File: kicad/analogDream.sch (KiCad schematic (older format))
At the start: 120 parts, among them P1 CONN_4X2, P10 CONN_7X2, P11 CONN_4X2, P12 CONN_4X2, P2 CONN_4X2, P3 CONN_7X2, P4 CONN_7X2, P5 CONN_4X2, P6 CONN_4X2, P7 CONN_4X2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

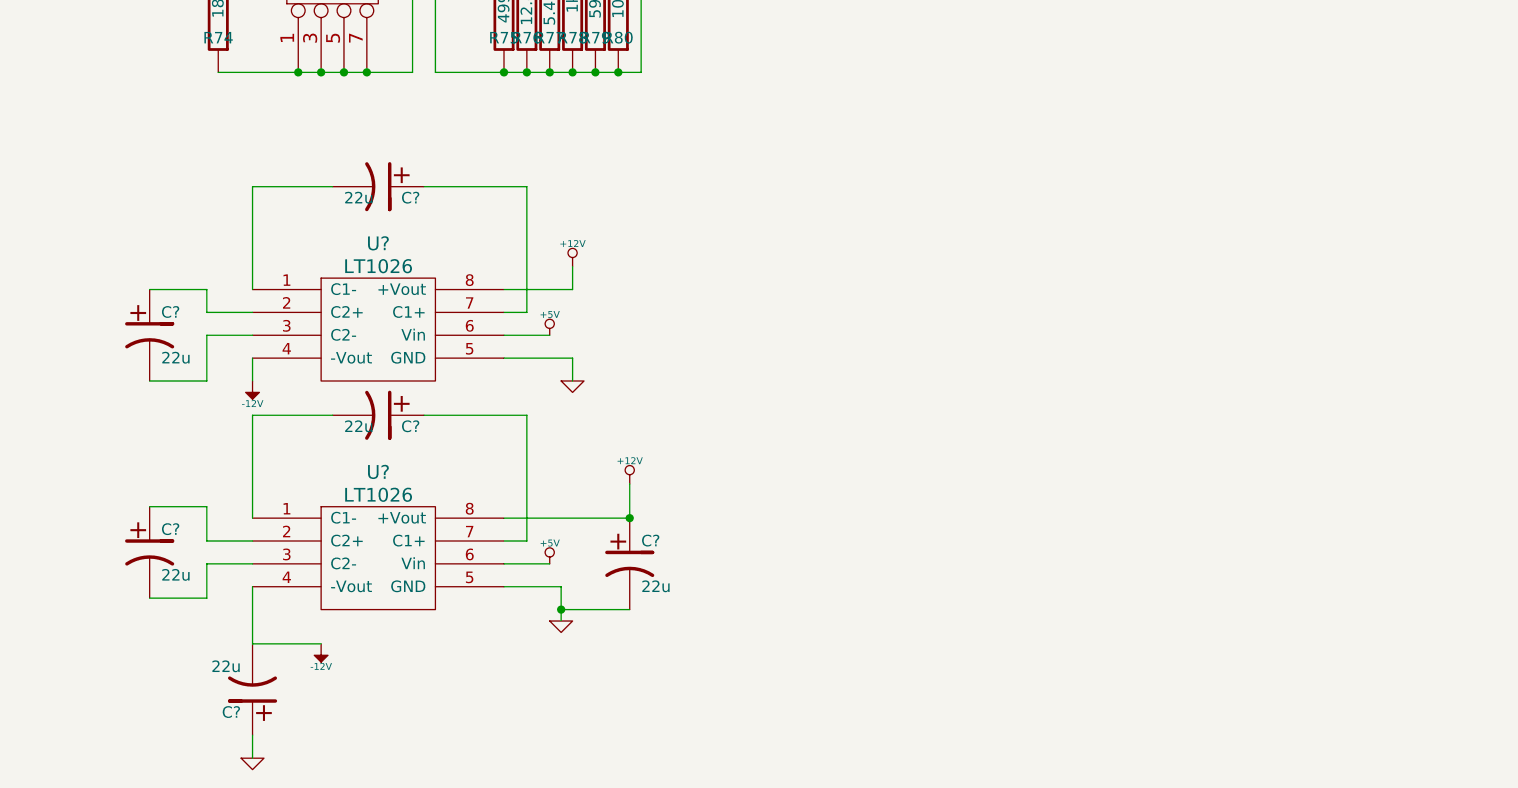
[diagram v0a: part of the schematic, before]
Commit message: Added input terminals
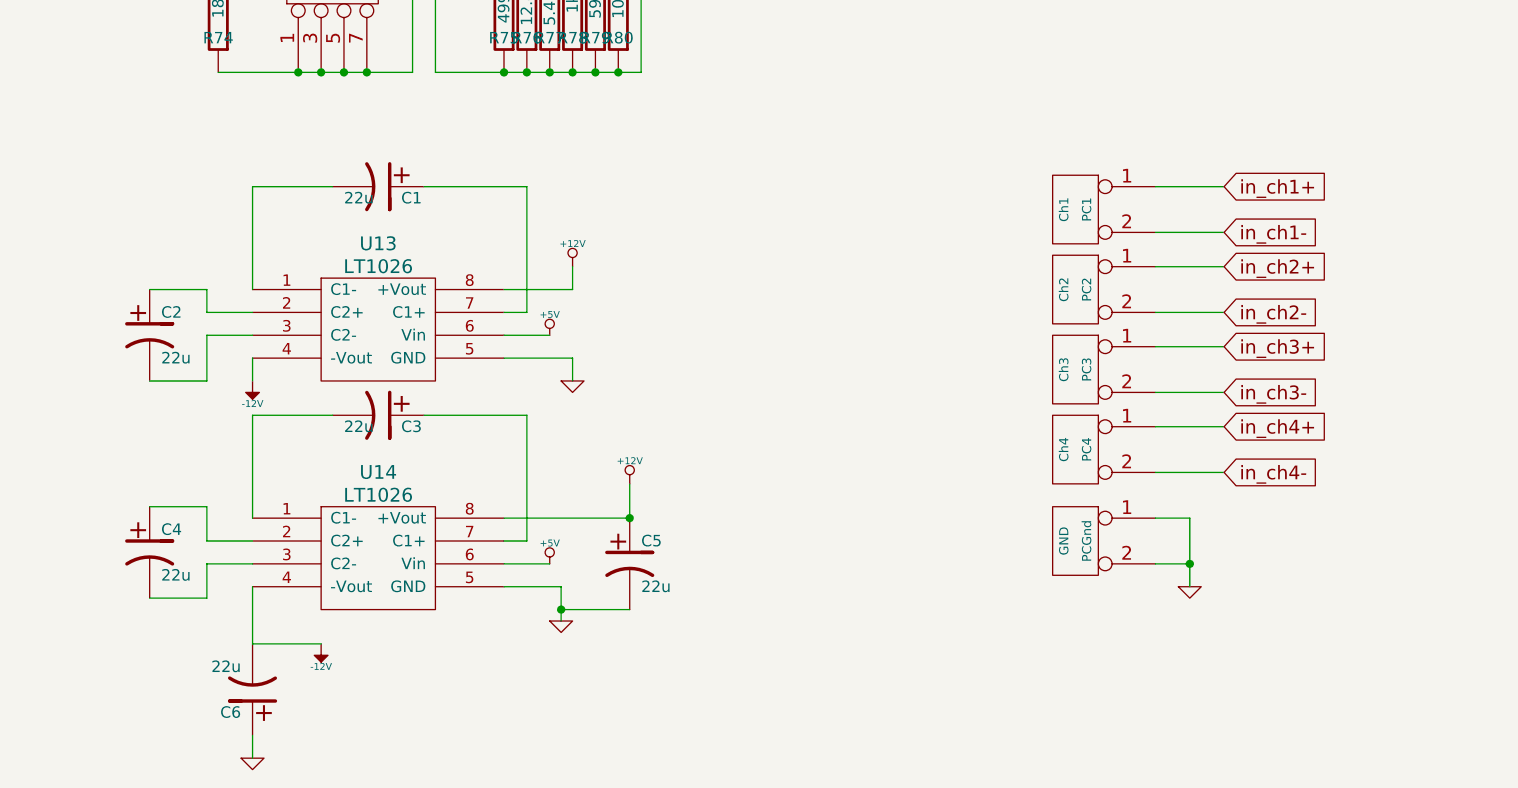
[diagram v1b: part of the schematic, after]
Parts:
- added PC1: Ch1, symbol CONN_2
- added PC2: Ch2, symbol CONN_2
- added PC3: Ch3, symbol CONN_2
- added PC4: Ch4, symbol CONN_2
- added PCGnd: GND, symbol CONN_2
- gave numbers to parts that had none: 8
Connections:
- wire segments 258 -> 269

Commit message: Worked on connecters
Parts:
- renumbered PCGnd to PC5

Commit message: Started working on pcb board
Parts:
- added PC6: out_1_2, symbol CONN_2
- added PC7: out_3_4, symbol CONN_2
- R28, R35, R68, R75: value 499k -> 49.9k
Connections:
- net labels added: out_ch1, out_ch2, out_ch3, out_ch4
- wire segments 269 -> 277

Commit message: Changed to dual opamp, changed pot resistors
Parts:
- removed U10, U11, U12, U3, U4, U5, U6, U9: TL071, symbol TL071
- added U2, U4, U6, U8: TL072, symbol TL072
- R1, R4, R42, R44: value 4.7k -> 47k
- R10, R15, R18, R20, R53, R55, R58, R60, RV1, RV2, RV3, RV4, RV5, RV6, RV7, RV8: value 1k -> 10k
- R45, R46, R5, R6: value 1.2k -> 12k
- renumbered U2 to U1, U14 to U10, U1 to U3, U8 to U5, U13 to U9

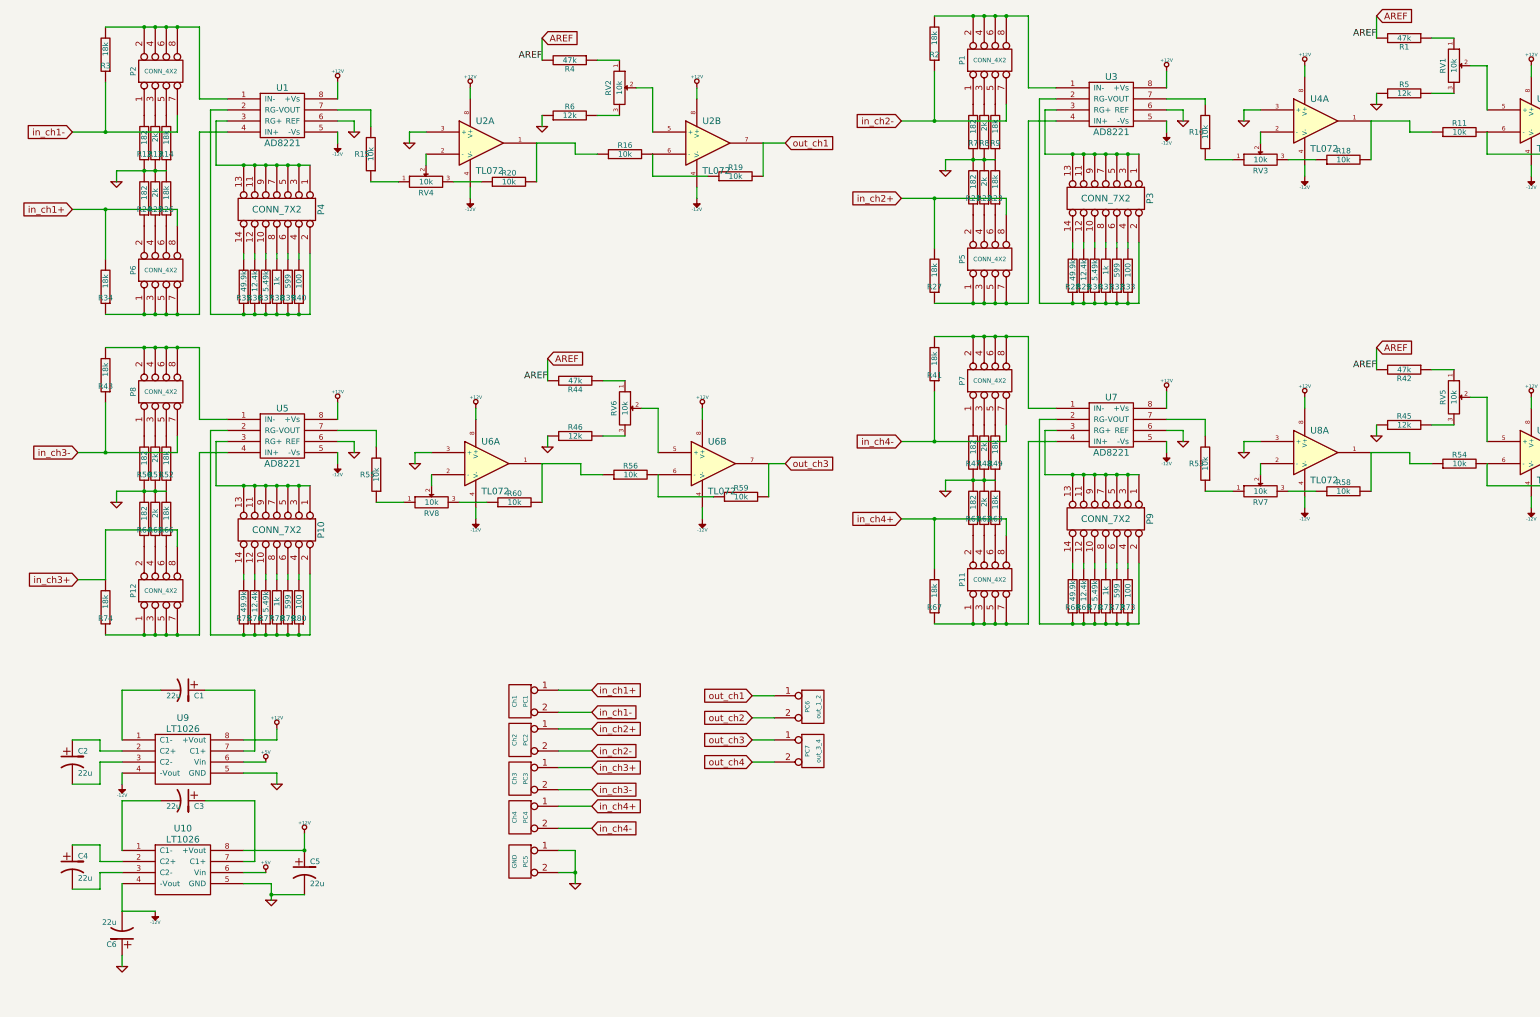
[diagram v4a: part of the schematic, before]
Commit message: Rotated pots, moved parts
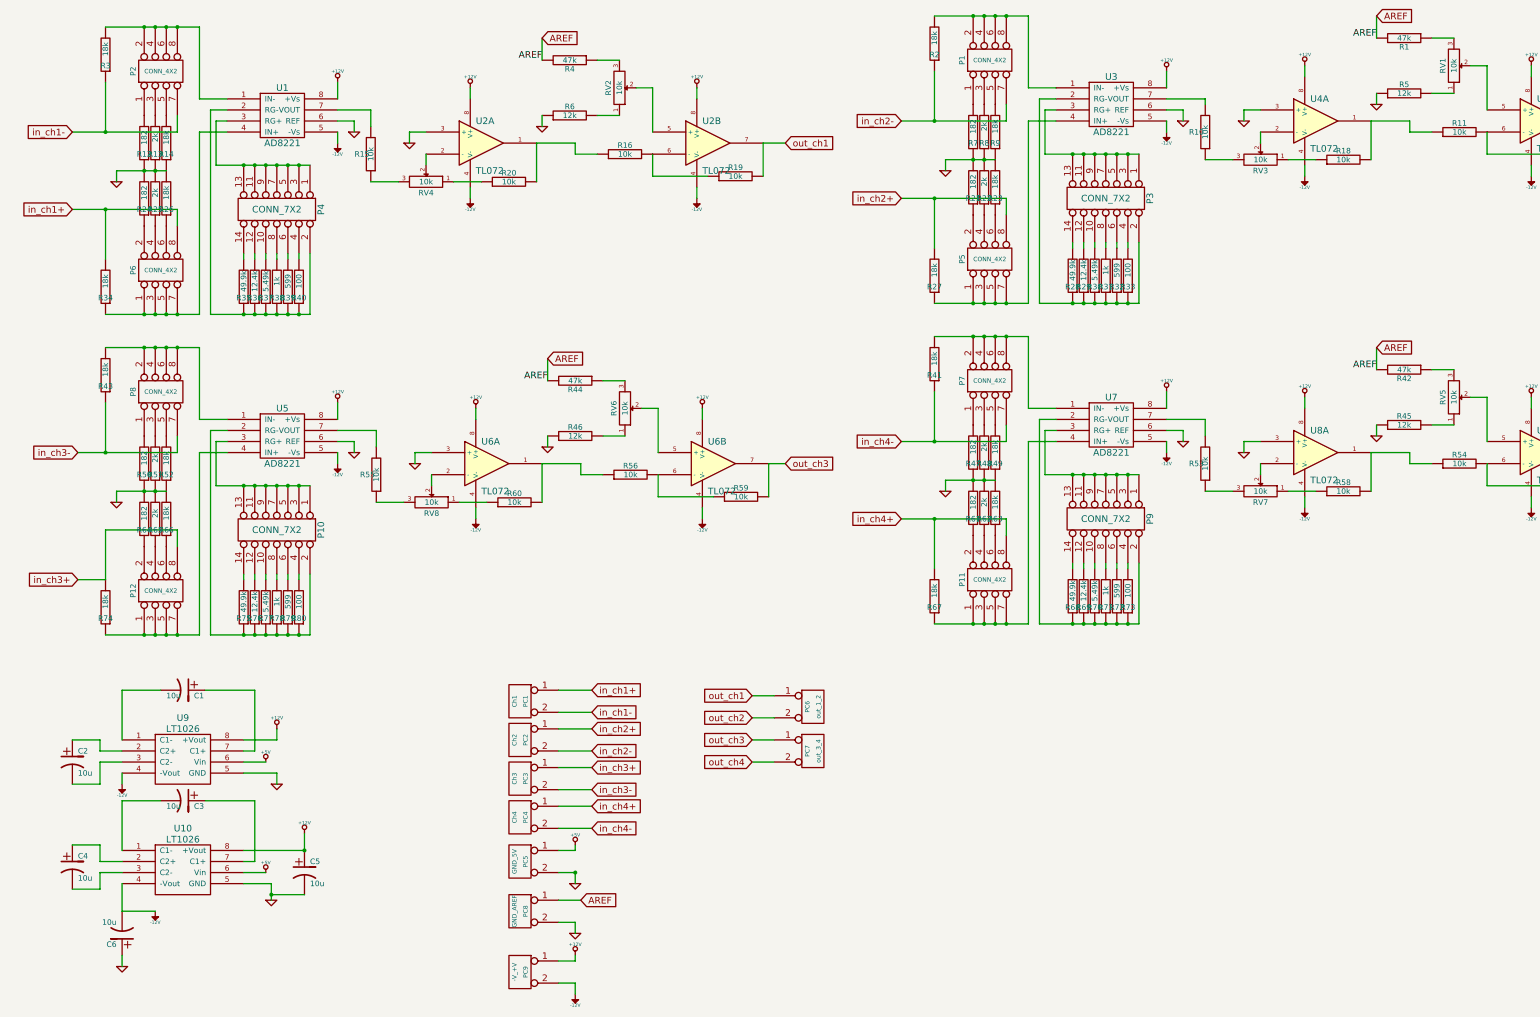
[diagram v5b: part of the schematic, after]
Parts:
- added PC8: GND_AREF, symbol CONN_2
- added PC9: -V_+V, symbol CONN_2
- C1, C2, C3, C4, C5, C6: value 22u -> 10u
- PC5: value GND -> GND_5V
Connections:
- net +12V: now also PC9.1 (P1)
- net +5V: now also PC5.1 (P1)
- net -12V: now also PC9.2 (PM)
- net AREF: now also PC8.1 (P1)
- net GND: now also PC8.2 (PM); no longer PC5.1 (P1)
- net at R15.1: now also RV4.3; no longer RV4.1
- net at R20.1: now also RV4.1; no longer RV4.3
- net at RV2.1: now also R6.2; no longer R4.1
- net at RV2.3: now also R4.1; no longer R6.2
- net at R44.1: now also RV6.3; no longer RV6.1
- net at R46.2: now also RV6.1; no longer RV6.3
- net at R60.1: now also RV8.1; no longer RV8.3
- net at R55.1: now also RV8.3; no longer RV8.1
- net at R10.1: now also RV3.3; no longer RV3.1
- net at R18.1: now also RV3.1; no longer RV3.3
- net at RV1.1: now also R5.2; no longer R1.1
- net at RV1.3: now also R1.1; no longer R5.2
- net at R53.1: now also RV7.3; no longer RV7.1
- net at R58.1: now also RV7.1; no longer RV7.3
- net at RV5.1: now also R45.2; no longer R42.1
- net at RV5.3: now also R42.1; no longer R45.2

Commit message: Fixed Pot, worked on silk screen
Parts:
- R32, R39, R72, R79: value 599 -> 499
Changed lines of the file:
@@
-EESchema Schematic File Version 2  date Sat 17 Dec 2011 09:17:39 PM MST
+EESchema Schematic File Version 2  date Fri 13 Jan 2012 09:39:40 PM MST
 LIBS:power
 LIBS:device
@@
 Sheet 1 1
 Title "Analog Dream Board"
-Date "18 dec 2011"
+Date "14 jan 2012"
 Rev ""
 Comp "Visgence Technologies"
@@
 P 10500 5850
 F 0 "R72" H 10500 5950 50  0000 C CNN
-F 1 "599" V 10500 5800 50  0000 C CNN
+F 1 "499" V 10500 5800 50  0000 C CNN
 	1    10500 5850
 	-1   0    0    1
@@
 P 10500 2950
 F 0 "R32" H 10500 3050 50  0000 C CNN
-F 1 "599" V 10500 2900 50  0000 C CNN
+F 1 "499" V 10500 2900 50  0000 C CNN
 	1    10500 2950
 	-1   0    0    1
@@
 P 3000 5950
 F 0 "R79" H 3000 6050 50  0000 C CNN
-F 1 "599" V 3000 5900 50  0000 C CNN
+F 1 "499" V 3000 5900 50  0000 C CNN
 	1    3000 5950
 	-1   0    0    1
@@
 P 3000 3050
 F 0 "R39" H 3000 3150 50  0000 C CNN
-F 1 "599" V 3000 3000 50  0000 C CNN
+F 1 "499" V 3000 3000 50  0000 C CNN
 	1    3000 3050
 	-1   0    0    1

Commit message: Fixed label for silk screen
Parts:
- PC5: value GND_5V -> 5V_GND
- PC8: value GND_AREF -> AREF_GND
- PC9: value -V_+V -> +V_-V
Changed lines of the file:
@@
-EESchema Schematic File Version 2  date Fri 13 Jan 2012 09:39:40 PM MST
+EESchema Schematic File Version 2  date 3/8/2012 1:42:21 PM
 LIBS:power
 LIBS:device
@@
 Sheet 1 1
 Title "Analog Dream Board"
-Date "14 jan 2012"
+Date "8 mar 2012"
 Rev ""
 Comp "Visgence Technologies"
@@
 P 5100 9250
 F 0 "PC9" V 5050 9250 40  0000 C CNN
-F 1 "-V_+V" V 5150 9250 40  0000 C CNN
+F 1 "+V_-V" V 5150 9250 40  0000 C CNN
 	1    5100 9250
 	-1   0    0    -1
@@
 P 5100 8700
 F 0 "PC8" V 5050 8700 40  0000 C CNN
-F 1 "GND_AREF" V 5150 8700 40  0000 C CNN
+F 1 "AREF_GND" V 5150 8700 40  0000 C CNN
 	1    5100 8700
 	-1   0    0    -1
@@
 P 5100 8250
 F 0 "PC5" V 5050 8250 40  0000 C CNN
-F 1 "GND_5V" V 5150 8250 40  0000 C CNN
+F 1 "5V_GND" V 5150 8250 40  0000 C CNN
 	1    5100 8250
 	-1   0    0    -1

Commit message: Changed to two channel round board
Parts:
- removed C1, C2: 10u, symbol CP1
- removed P10, P9: CONN_7X2, symbol CONN_7X2
- removed P11, P12, P7, P8: CONN_4X2, symbol CONN_4X2
- removed PC3: Ch3, symbol CONN_2
- removed PC4: Ch4, symbol CONN_2
- removed PC7: out_3_4, symbol CONN_2
- removed R41, R43, R49, R52, R63, R66, R67, R74: 18k, symbol R
- removed R42, R44: 47k, symbol R
- removed R45, R46: 12k, symbol R
- removed R47, R50, R61, R64: 182, symbol R
- removed R48, R51, R62, R65: 2k, symbol R
- removed R53, R54, R55, R56, R57, R58, R59, R60: 10k, symbol R
- removed R68, R75: 49.9k, symbol R
- removed R69, R76: 12.4k, symbol R
- removed R70, R77: 5.49k, symbol R
- removed R71, R78: 1k, symbol R
- removed R72, R79: 499, symbol R
- removed R73, R80: 100, symbol R
- removed RV5, RV6, RV7, RV8: 10k, symbol POT
- removed U5, U7: AD8221, symbol AD8221
- removed U6, U8: TL072, symbol TL072
- removed U9: LT1026, symbol LT1026
- added C1, C2, C7: 220n, symbol C
- added K1: RefJump, symbol CONN_3
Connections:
- net +12V: now also C2.2
- net +5V: now also K1.1 (P1)
- net -12V: now also C1.2
- net AREF: now also C7.2, K1.2 (PM); no longer PC8.1 (P1)
- net GND: now also C1.1, C2.1, C7.1
- net at U10.1 (C1-): now also C3.1, U10.7 (C1+); no longer C3.2
- new net: K1.3 (P3), PC8.1 (P1)
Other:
- moved on the sheet: C3, C4, C5, C6, PC1, PC2, PC5, PC6, PC8, PC9, U10
